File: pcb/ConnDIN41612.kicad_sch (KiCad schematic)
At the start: 44 parts, among them IC1 SN65HVD75DR, J1 DIN41612_02x32_AC, T1 H1102NL, U3 USBLC6-2SC6, U4 USBLC6-2SC6, U5 USBLC6-2SC6

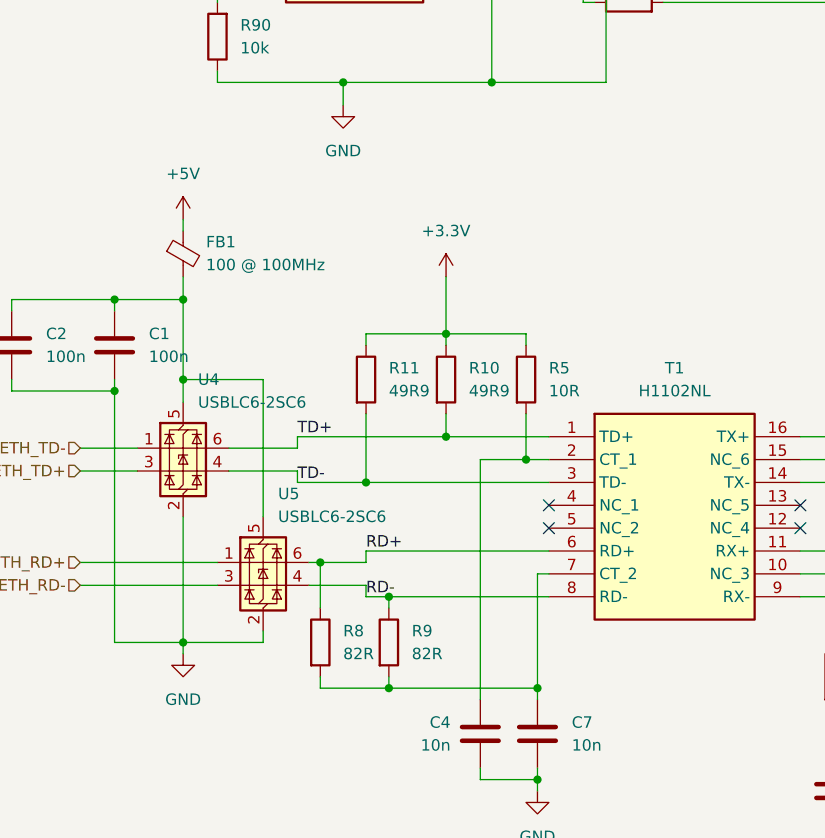
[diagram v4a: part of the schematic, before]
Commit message: Corected mistakes found on RDE_board
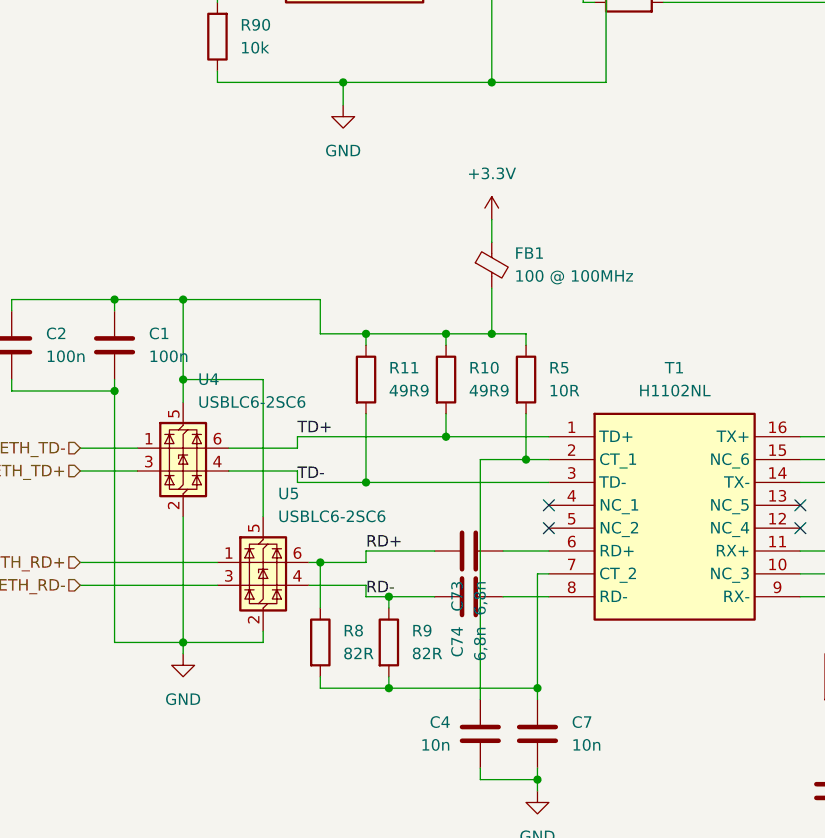
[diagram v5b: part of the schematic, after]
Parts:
- added C73, C74: 6,8n, Capacitor_SMD:C_0603_1608Metric_Pad1.08x0.95mm_HandSolder, symbol Device:C
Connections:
- net +3.3V: now also FB1.1; no longer R10.1, R11.1, R5.1
- net +5V: no longer FB1.1
- net RD+: now also C73.2; no longer T1.6 (RD+)
- net RD-: now also C74.2; no longer T1.8 (RD-)
- net at C1.1, C2.1, FB1.2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: now also R10.1, R11.1, R5.1
- new net: C73.1, T1.6 (RD+)
- new net: C74.1, T1.8 (RD-)
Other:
- moved on the sheet: FB1
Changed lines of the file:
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@@
 	)
 	(junction
+		(at 85.09 128.27)
+		(diameter 0)
+		(color 0 0 0 0)
+	)
+	(junction
 		(at 226.06 101.6)
 		(diameter 0)
@@
 	)
 	(junction
-		(at 50.8 124.46)
-		(diameter 0)
-		(color 0 0 0 0)
-	)
-	(junction
 		(at 80.01 139.7)
 		(diameter 0)
@@
 	)
 	(junction
+		(at 50.8 124.46)
+		(diameter 0)
+		(color 0 0 0 0)
+	)
+	(junction
 		(at 219.71 50.8)
 		(diameter 0)
@@
 		(color 0 0 0 0)
 	)
+	(junction
+		(at 71.12 128.27)
+		(diameter 0)
+		(color 0 0 0 0)
+	)
 	(no_connect
 		(at 91.44 147.32)
@@
 	(wire
 		(pts
+			(xy 85.09 128.27) (xy 88.9 128.27)
+		)
+		(stroke
+			(width 0)
+			(type default)
+		)
+	)
+	(wire
+		(pts
 			(xy 50.8 40.64) (xy 53.34 40.64)
 		)
@@
 	(wire
 		(pts
+			(xy 86.36 152.4) (xy 91.44 152.4)
+		)
+		(stroke
+			(width 0)
+			(type default)
+		)
+	)
+	(wire
+		(pts
 			(xy 54.61 86.36) (xy 57.15 86.36)
 		)
@@
 	(wire
 		(pts
-			(xy 73.66 157.48) (xy 91.44 157.48)
+			(xy 73.66 157.48) (xy 78.74 157.48)
 		)
 		(stroke
@@
 	(wire
 		(pts
+			(xy 86.36 157.48) (xy 91.44 157.48)
+		)
+		(stroke
+			(width 0)
+			(type default)
+		)
+	)
+	(wire
+		(pts
 			(xy 256.54 66.04) (xy 256.54 67.31)
 		)
@@
 	(wire
 		(pts
-			(xy 50.8 121.92) (xy 50.8 124.46)
+			(xy 85.09 123.19) (xy 85.09 128.27)
 		)
 		(stroke
@@
 	(wire
 		(pts
-			(xy 71.12 152.4) (xy 91.44 152.4)
+			(xy 71.12 152.4) (xy 78.74 152.4)
 		)
 		(stroke
@@
 	(wire
 		(pts
+			(xy 66.04 128.27) (xy 71.12 128.27)
+		)
+		(stroke
+			(width 0)
+			(type default)
+		)
+	)
+	(wire
+		(pts
 			(xy 54.61 83.82) (xy 57.15 83.82)
 		)
@@
 	(wire
 		(pts
+			(xy 50.8 124.46) (xy 66.04 124.46)
+		)
+		(stroke
+			(width 0)
+			(type default)
+		)
+	)
+	(wire
+		(pts
 			(xy 63.5 140.97) (xy 63.5 139.7)
 		)
@@
 	(wire
 		(pts
-			(xy 50.8 115.57) (xy 50.8 116.84)
+			(xy 265.43 35.56) (xy 265.43 58.42)
 		)
 		(stroke
@@
 	(wire
 		(pts
-			(xy 265.43 35.56) (xy 265.43 58.42)
+			(xy 165.1 43.18) (xy 165.1 53.34)
 		)
 		(stroke
@@
 	(wire
 		(pts
-			(xy 165.1 43.18) (xy 165.1 53.34)
+			(xy 85.09 88.9) (xy 85.09 100.33)
 		)
 		(stroke
@@
 	(wire
 		(pts
-			(xy 85.09 88.9) (xy 85.09 100.33)
+			(xy 119.38 139.7) (xy 149.86 139.7)
 		)
 		(stroke
@@
 	(wire
 		(pts
-			(xy 119.38 139.7) (xy 149.86 139.7)
+			(xy 60.96 40.64) (xy 74.93 40.64)
 		)
 		(stroke
@@
 	(wire
 		(pts
-			(xy 60.96 40.64) (xy 74.93 40.64)
+			(xy 66.04 124.46) (xy 66.04 128.27)
 		)
 		(stroke
@@
 	(wire
 		(pts
-			(xy 80.01 121.92) (xy 80.01 128.27)
+			(xy 85.09 115.57) (xy 85.09 118.11)
 		)
 		(stroke
@@
 	(wire
 		(pts
-			(xy 80.01 128.27) (xy 88.9 128.27)
+			(xy 80.01 128.27) (xy 85.09 128.27)
 		)
 		(stroke
@@
 	(symbol
 		(lib_id "power:+3.3V")
-		(at 80.01 121.92 0)
+		(at 85.09 115.57 0)
 		(unit 1)
 		(exclude_from_sim no)
@@
 		(fields_autoplaced yes)
 		(property "Reference" "#PWR024"
-			(at 80.01 125.73 0)
+			(at 85.09 119.38 0)
 			(effects
 				(font
@@
 		)
 		(property "Value" "+3.3V"
-			(at 80.01 116.84 0)
+			(at 85.09 110.49 0)
 			(effects
 				(font
@@
 		)
 		(property "Footprint" ""
-			(at 80.01 121.92 0)
+			(at 85.09 115.57 0)
 			(effects
 				(font
@@
 		)
 		(property "Datasheet" ""
-			(at 80.01 121.92 0)
+			(at 85.09 115.57 0)
 			(effects
 				(font
@@
 		)
 		(property "Description" "Power symbol creates a global label with name \"+3.3V\""
-			(at 80.01 121.92 0)
+			(at 85.09 115.57 0)
 			(effects
 				(font
@@
 	(symbol
 		(lib_id "Device:FerriteBead_Small")
-		(at 50.8 119.38 0)
+		(at 85.09 120.65 0)
 		(unit 1)
 		(exclude_from_sim no)
@@
 		(fields_autoplaced yes)
 		(property "Reference" "FB1"
-			(at 53.34 118.0718 0)
+			(at 87.63 119.3418 0)
 			(effects
 				(font
@@
 		)
 		(property "Value" "100 @ 100MHz"
-			(at 53.34 120.6118 0)
+			(at 87.63 121.8818 0)
 			(effects
 				(font
@@
 		)
 		(property "Footprint" "Inductor_SMD:L_0603_1608Metric_Pad1.05x0.95mm_HandSolder"
-			(at 49.022 119.38 90)
+			(at 83.312 120.65 90)
 			(effects
 				(font
@@
 		)
 		(property "Datasheet" "~"
-			(at 50.8 119.38 0)
+			(at 85.09 120.65 0)
 			(effects
 				(font
@@
 		)
 		(property "Description" "WLBD1608HCU101TL"
-			(at 50.8 119.38 0)
+			(at 85.09 120.65 0)
 			(effects
 				(font
@@
 	)
 	(symbol
+		(lib_id "Device:C")
+		(at 82.55 152.4 270)
+		(unit 1)
+		(exclude_from_sim no)
+		(in_bom yes)
+		(on_board yes)
+		(dnp no)
+		(property "Reference" "C73"
+			(at 81.28 155.702 0)
+			(effects
+				(font
+					(size 1.27 1.27)
+				)
+				(justify left)
+			)
+		)
+		(property "Value" "6,8n"
+			(at 83.82 155.702 0)
+			(effects
+				(font
+					(size 1.27 1.27)
+				)
+				(justify left)
+			)
+		)
+		(property "Footprint" "Capacitor_SMD:C_0603_1608Metric_Pad1.08x0.95mm_HandSolder"
+			(at 78.74 153.3652 0)
+			(effects
+				(font
+					(size 1.27 1.27)
+				)
+				(hide yes)
+			)
+		)
+		(property "Datasheet" "~"
+			(at 82.55 152.4 0)
+			(effects
+				(font
+					(size 1.27 1.27)
+				)
+				(hide yes)
+			)
+		)
+		(property "Description" "Unpolarized capacitor"
+			(at 82.55 152.4 0)
+			(effects
+				(font
+					(size 1.27 1.27)
+				)
+				(hide yes)
+			)
+		)
+		(pin "1"
+		)
+		(pin "2"
+		)
+		(instances
+			(project "UCB_board"
+				(path "/0c4edb77-9bdf-4103-be66-c5eb9940b163/8ab86091-8037-4e58-8522-0946e4707b6d"
+					(reference "C73")
+					(unit 1)
+				)
+			)
+		)
+	)
+	(symbol
 		(lib_id "power:GND")
 		(at 241.3 144.78 0)
@@
 	)
 	(symbol
-		(lib_id "power:+5V")
-		(at 50.8 115.57 0)
-		(unit 1)
-		(exclude_from_sim no)
-		(in_bom yes)
-		(on_board yes)
-		(dnp no)
-		(fields_autoplaced yes)
-		(property "Reference" "#PWR017"
-			(at 50.8 119.38 0)
-			(effects
-				(font
-					(size 1.27 1.27)
-				)
-				(hide yes)
-			)
-		)
-		(property "Value" "+5V"
-			(at 50.8 110.49 0)
-			(effects
-				(font
-					(size 1.27 1.27)
-				)
-			)
-		)
-		(property "Footprint" ""
-			(at 50.8 115.57 0)
-			(effects
-				(font
-					(size 1.27 1.27)
-				)
-				(hide yes)
-			)
-		)
-		(property "Datasheet" ""
-			(at 50.8 115.57 0)
-			(effects
-				(font
-					(size 1.27 1.27)
-				)
-				(hide yes)
-			)
-		)
-		(property "Description" "Power symbol creates a global label with name \"+5V\""
-			(at 50.8 115.57 0)
-			(effects
-				(font
-					(size 1.27 1.27)
-				)
-				(hide yes)
-			)
-		)
-		(pin "1"
-		)
-		(instances
-			(project "100x100_eurocard_testboard"
-				(path "/0c4edb77-9bdf-4103-be66-c5eb9940b163/8ab86091-8037-4e58-8522-0946e4707b6d"
-					(reference "#PWR017")
-					(unit 1)
-				)
-			)
-		)
-	)
-	(symbol
 		(lib_id "Device:R")
 		(at 123.19 166.37 0)
@@
 					(unit 1)
 				)
+			)
+		)
+	)
+	(symbol
+		(lib_id "Device:C")
+		(at 82.55 157.48 270)
+		(unit 1)
+		(exclude_from_sim no)
+		(in_bom yes)
+		(on_board yes)
+		(dnp no)
+		(property "Reference" "C74"
+			(at 81.28 160.782 0)
+			(effects
+				(font
+					(size 1.27 1.27)
+				)
+				(justify left)
+			)
+		)
+		(property "Value" "6,8n"
+			(at 83.82 160.782 0)
+			(effects
+				(font
+					(size 1.27 1.27)
+				)
+				(justify left)
+			)
+		)
+		(property "Footprint" "Capacitor_SMD:C_0603_1608Metric_Pad1.08x0.95mm_HandSolder"
+			(at 78.74 158.4452 0)
+			(effects
+				(font
+					(size 1.27 1.27)
+				)
+				(hide yes)
+			)
+		)
+		(property "Datasheet" "~"
+			(at 82.55 157.48 0)
+			(effects
+				(font
+					(size 1.27 1.27)
+				)
+				(hide yes)
+			)
+		)
+		(property "Description" "Unpolarized capacitor"
+			(at 82.55 157.48 0)
+			(effects
+				(font
+					(size 1.27 1.27)
+				)
+				(hide yes)
+			)
+		)
+		(pin "1"
+		)
+		(pin "2"
+		)
+		(instances
+			(project "UCB_board"
+				(path "/0c4edb77-9bdf-4103-be66-c5eb9940b163/8ab86091-8037-4e58-8522-0946e4707b6d"
+					(reference "C74")
+					(unit 1)
+				)
